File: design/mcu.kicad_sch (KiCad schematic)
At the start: 35 parts, among them J2 SWD_01X06, J3 DEBUG_SPI, U6 STM32H750VBTx, X1 ASTX-H11-25.000MHZ-T, X2 SIT8209AI-21-33S-100.000000X

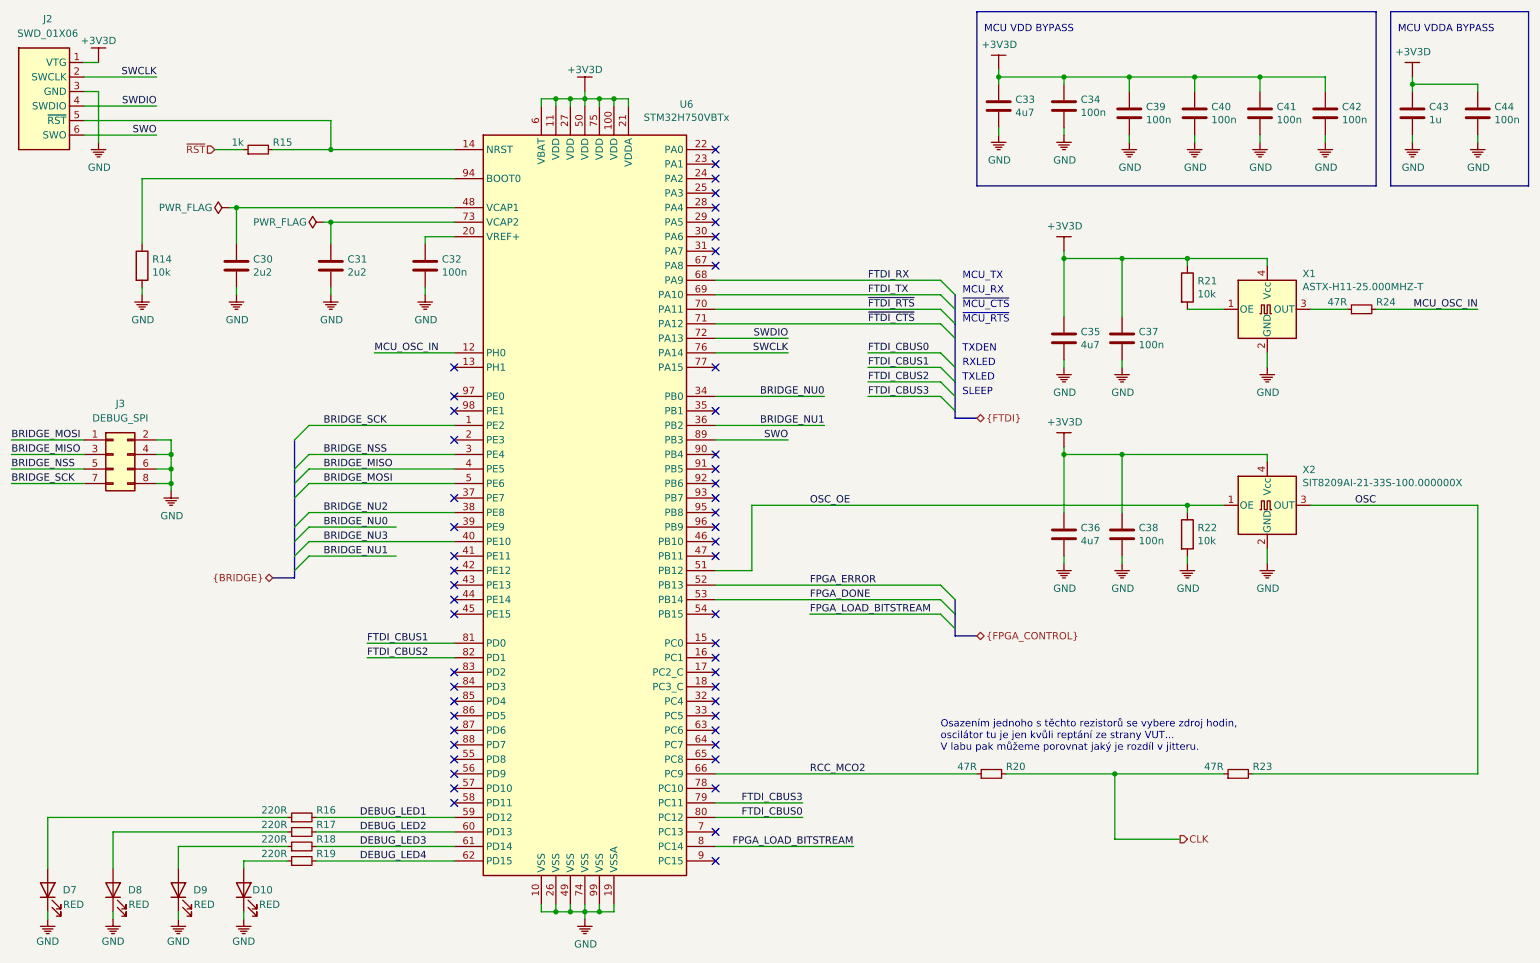
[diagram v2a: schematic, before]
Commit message: Updated reset system
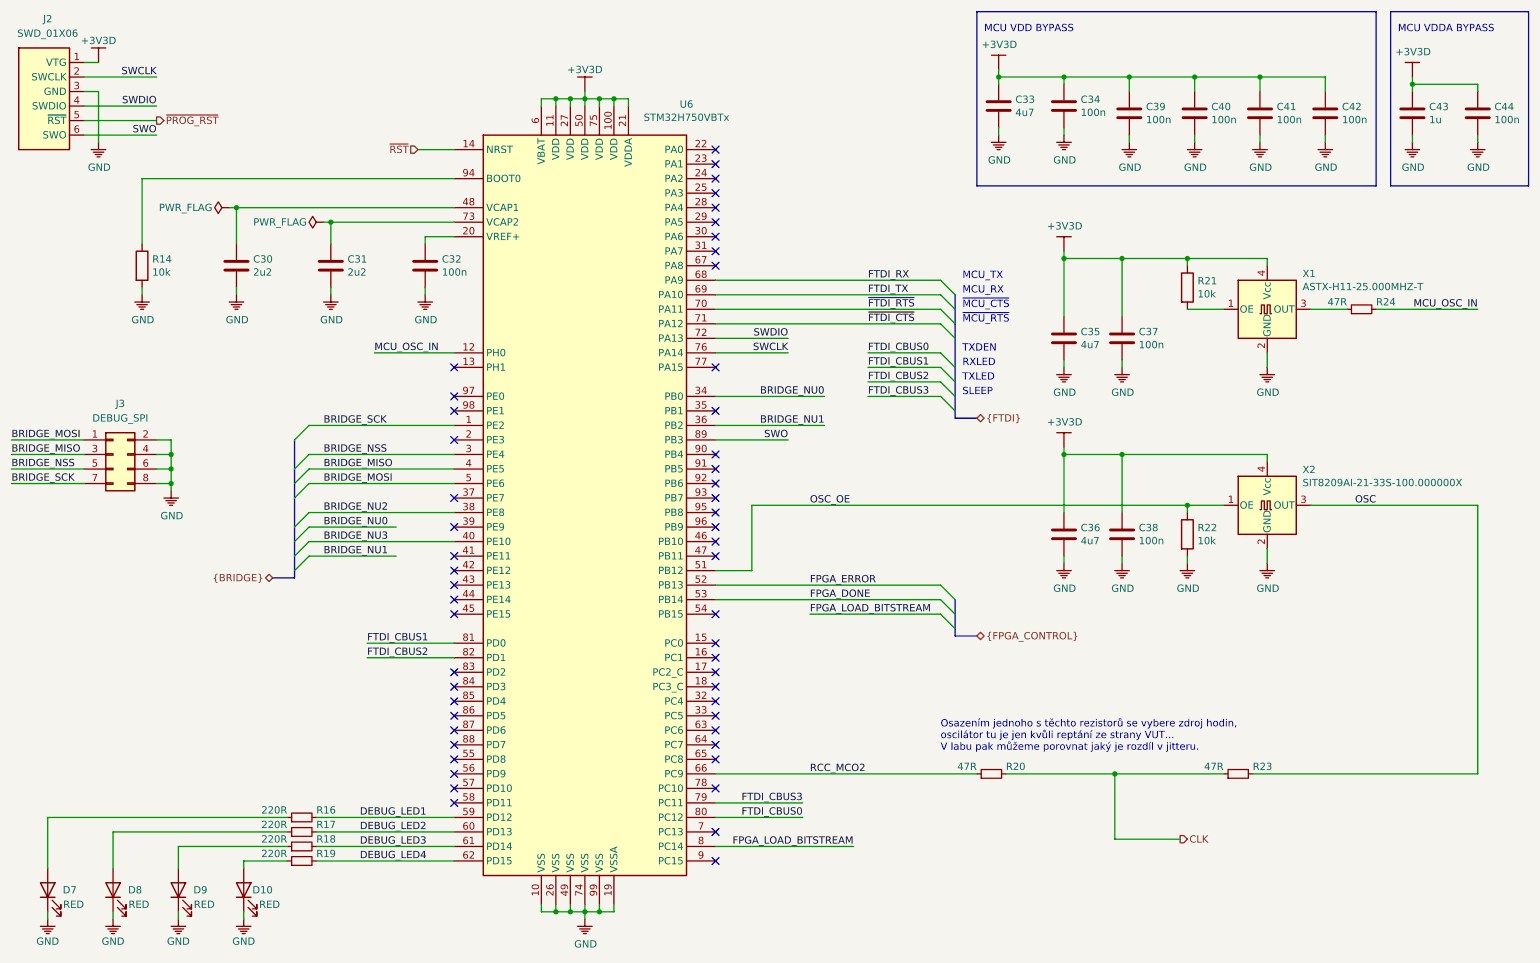
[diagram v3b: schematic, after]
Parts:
- removed R15: 1k, Resistor_SMD:R_0603_1608Metric, symbol Device:R_Small
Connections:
- net ~RST: now also U6.14 (NRST)
- net ~PROG_RST: now reaches J2.5 (~RST)
- net ~PROG_RST: no longer U6.14 (NRST)
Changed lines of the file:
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@@
   (junction (at 45.72 96.52))
   (junction (at 57.15 48.26))
-  (junction (at 73.66 38.1))
   (junction (at 73.66 50.8))
   (junction (at 113.03 29.21))
@@
   (junction (at 236.22 25.4))
   (junction (at 262.89 26.67))
+  (no_connect (at 140.97 43.18))
+  (no_connect (at 140.97 104.14))
+  (no_connect (at 140.97 149.86))
+  (no_connect (at 95.25 139.7))
+  (no_connect (at 95.25 99.06))
+  (no_connect (at 95.25 109.22))
+  (no_connect (at 140.97 134.62))
+  (no_connect (at 140.97 129.54))
+  (no_connect (at 140.97 142.24))
+  (no_connect (at 95.25 134.62))
+  (no_connect (at 95.25 149.86))
+  (no_connect (at 140.97 93.98))
+  (no_connect (at 140.97 53.34))
+  (no_connect (at 140.97 137.16))
+  (no_connect (at 95.25 144.78))
+  (no_connect (at 140.97 76.2))
+  (no_connect (at 95.25 116.84))
+  (no_connect (at 140.97 91.44))
+  (no_connect (at 140.97 38.1))
+  (no_connect (at 95.25 152.4))
+  (no_connect (at 95.25 119.38))
+  (no_connect (at 95.25 137.16))
+  (no_connect (at 140.97 99.06))
+  (no_connect (at 140.97 96.52))
+  (no_connect (at 140.97 124.46))
   (no_connect (at 140.97 45.72))
-  (no_connect (at 140.97 129.54))
-  (no_connect (at 95.25 109.22))
-  (no_connect (at 140.97 93.98))
+  (no_connect (at 140.97 132.08))
+  (no_connect (at 95.25 81.28))
+  (no_connect (at 95.25 104.14))
+  (no_connect (at 95.25 83.82))
+  (no_connect (at 140.97 55.88))
+  (no_connect (at 95.25 111.76))
+  (no_connect (at 140.97 127))
+  (no_connect (at 140.97 50.8))
+  (no_connect (at 140.97 157.48))
+  (no_connect (at 95.25 142.24))
+  (no_connect (at 95.25 76.2))
+  (no_connect (at 140.97 106.68))
+  (no_connect (at 140.97 48.26))
+  (no_connect (at 95.25 88.9))
+  (no_connect (at 140.97 40.64))
+  (no_connect (at 140.97 162.56))
+  (no_connect (at 140.97 109.22))
+  (no_connect (at 140.97 83.82))
+  (no_connect (at 95.25 147.32))
+  (no_connect (at 140.97 144.78))
+  (no_connect (at 140.97 101.6))
+  (no_connect (at 140.97 139.7))
+  (no_connect (at 95.25 114.3))
   (no_connect (at 95.25 132.08))
-  (no_connect (at 95.25 104.14))
-  (no_connect (at 140.97 48.26))
-  (no_connect (at 140.97 53.34))
-  (no_connect (at 140.97 142.24))
-  (no_connect (at 95.25 139.7))
-  (no_connect (at 140.97 139.7))
-  (no_connect (at 140.97 157.48))
-  (no_connect (at 140.97 106.68))
-  (no_connect (at 140.97 127))
-  (no_connect (at 140.97 137.16))
-  (no_connect (at 140.97 38.1))
-  (no_connect (at 140.97 99.06))
-  (no_connect (at 95.25 83.82))
-  (no_connect (at 95.25 88.9))
-  (no_connect (at 140.97 55.88))
-  (no_connect (at 95.25 81.28))
-  (no_connect (at 140.97 50.8))
-  (no_connect (at 95.25 134.62))
-  (no_connect (at 140.97 91.44))
-  (no_connect (at 140.97 96.52))
-  (no_connect (at 140.97 162.56))
-  (no_connect (at 95.25 76.2))
-  (no_connect (at 95.25 137.16))
+  (no_connect (at 140.97 119.38))
   (no_connect (at 95.25 129.54))
-  (no_connect (at 140.97 43.18))
-  (no_connect (at 95.25 149.86))
-  (no_connect (at 95.25 111.76))
-  (no_connect (at 140.97 76.2))
-  (no_connect (at 140.97 149.86))
-  (no_connect (at 140.97 119.38))
-  (no_connect (at 140.97 134.62))
-  (no_connect (at 140.97 104.14))
-  (no_connect (at 95.25 144.78))
-  (no_connect (at 140.97 144.78))
-  (no_connect (at 95.25 152.4))
-  (no_connect (at 140.97 132.08))
-  (no_connect (at 140.97 109.22))
-  (no_connect (at 140.97 101.6))
   (no_connect (at 140.97 58.42))
-  (no_connect (at 95.25 142.24))
-  (no_connect (at 95.25 114.3))
-  (no_connect (at 95.25 147.32))
-  (no_connect (at 140.97 83.82))
-  (no_connect (at 95.25 99.06))
-  (no_connect (at 95.25 116.84))
-  (no_connect (at 95.25 119.38))
-  (no_connect (at 140.97 124.46))
-  (no_connect (at 140.97 40.64))
   (bus_entry (at 67.31 88.9) (size 2.54 -2.54))
   (bus_entry (at 67.31 93.98) (size 2.54 -2.54))
@@
   (wire (pts (xy 30.48 25.4) (xy 43.18 25.4)))
   (wire (pts (xy 30.48 30.48) (xy 43.18 30.48)))
-  (wire (pts (xy 30.48 33.02) (xy 73.66 33.02)))
+  (wire (pts (xy 30.48 33.02) (xy 43.18 33.02)))
   (wire (pts (xy 30.48 35.56) (xy 43.18 35.56)))
   (wire (pts (xy 33.02 27.94) (xy 30.48 27.94)))
@@
   (wire (pts (xy 46.99 160.02) (xy 46.99 163.83)))
   (wire (pts (xy 46.99 171.45) (xy 46.99 172.72)))
-  (wire (pts (xy 53.34 38.1) (xy 58.42 38.1)))
   (wire (pts (xy 55.88 48.26) (xy 57.15 48.26)))
   (wire (pts (xy 57.15 48.26) (xy 57.15 54.61)))
@@
   (wire (pts (xy 58.42 162.56) (xy 58.42 163.83)))
   (wire (pts (xy 58.42 171.45) (xy 58.42 172.72)))
-  (wire (pts (xy 63.5 38.1) (xy 73.66 38.1)))
   (wire (pts (xy 66.04 154.94) (xy 24.13 154.94)))
   (wire (pts (xy 66.04 157.48) (xy 35.56 157.48)))
@@
   (wire (pts (xy 69.85 109.22) (xy 85.09 109.22)))
   (wire (pts (xy 72.39 50.8) (xy 73.66 50.8)))
-  (wire (pts (xy 73.66 33.02) (xy 73.66 38.1)))
-  (wire (pts (xy 73.66 38.1) (xy 95.25 38.1)))
   (wire (pts (xy 73.66 50.8) (xy 73.66 54.61)))
   (wire (pts (xy 73.66 50.8) (xy 95.25 50.8)))
@@
   (wire (pts (xy 80.01 127) (xy 95.25 127)))
   (wire (pts (xy 81.28 73.66) (xy 95.25 73.66)))
+  (wire (pts (xy 88.9 38.1) (xy 95.25 38.1)))
   (wire (pts (xy 90.17 53.34) (xy 95.25 53.34)))
   (wire (pts (xy 90.17 54.61) (xy 90.17 53.34)))
@@
   (bus (pts (xy 63.5 113.03) (xy 67.31 113.03)))
   (bus (pts (xy 67.31 88.9) (xy 67.31 96.52)))
-  (bus (pts (xy 67.31 96.52) (xy 67.31 104.14)))
-  (bus (pts (xy 67.31 104.14) (xy 67.31 109.22)))
-  (bus (pts (xy 67.31 109.22) (xy 67.31 113.03)))
+  (bus (pts (xy 67.31 96.52) (xy 67.31 99.06)))
+  (bus (pts (xy 67.31 99.06) (xy 67.31 106.68)))
+  (bus (pts (xy 67.31 106.68) (xy 67.31 111.76)))
+  (bus (pts (xy 67.31 111.76) (xy 67.31 113.03)))
   (bus (pts (xy 182.88 63.5) (xy 182.88 68.58)))
   (bus (pts (xy 182.88 68.58) (xy 182.88 76.2)))
-  (bus (pts (xy 182.88 76.2) (xy 182.88 78.74)))
-  (bus (pts (xy 182.88 78.74) (xy 182.88 83.82)))
-  (bus (pts (xy 182.88 83.82) (xy 182.88 85.09)))
+  (bus (pts (xy 182.88 76.2) (xy 182.88 81.28)))
+  (bus (pts (xy 182.88 81.28) (xy 182.88 85.09)))
   (bus (pts (xy 182.88 85.09) (xy 186.69 85.09)))
-  (bus (pts (xy 182.88 116.84) (xy 182.88 119.38)))
-  (bus (pts (xy 182.88 119.38) (xy 182.88 123.19)))
+  (bus (pts (xy 182.88 116.84) (xy 182.88 121.92)))
+  (bus (pts (xy 182.88 121.92) (xy 182.88 123.19)))
   (bus (pts (xy 186.69 123.19) (xy 182.88 123.19)))
   (polyline (pts (xy 186.69 13.97) (xy 186.69 44.45)))
@@
     (effects (font (size 1.27 1.27)) (justify right bottom))
   )
-  (hierarchical_label "~RST" (shape input) (at 53.34 38.1 180)
-    (effects (font (size 1.27 1.27)) (justify right))
+  (hierarchical_label "~PROG_RST" (shape output) (at 43.18 33.02 0)
+    (effects (font (size 1.27 1.27)) (justify left))
   )
   (hierarchical_label "{BRIDGE}" (shape bidirectional) (at 63.5 113.03 180)
     (effects (font (size 1.27 1.27)) (justify right))
   )
+  (hierarchical_label "~RST" (shape input) (at 88.9 38.1 180)
+    (effects (font (size 1.27 1.27)) (justify right))
+  )
   (hierarchical_label "{FTDI}" (shape bidirectional) (at 186.69 85.09 0)
     (effects (font (size 1.27 1.27)) (justify left))
@@
       (effects (font (size 1.27 1.27)) hide)
     )
-  )
-  (symbol (lib_name "Device:R_Small_1") (lib_id "Device:R_Small") (at 60.96 38.1 90) (unit 1)
-    (property "Reference" "R15" (id 0) (at 63.5 36.83 90)
-      (effects (font (size 1.27 1.27)) (justify right))
-    )
-    (property "Value" "1k" (id 1) (at 58.42 36.83 90)
-      (effects (font (size 1.27 1.27)) (justify left))
-    )
-    (property "Footprint" "Resistor_SMD:R_0603_1608Metric" (id 2) (at 60.96 38.1 0)
-      (effects (font (size 1.27 1.27)) hide)
-    )
-    (property "Datasheet" "~" (id 3) (at 60.96 38.1 0)
-      (effects (font (size 1.27 1.27)) hide)
-    )

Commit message: Added fiducials
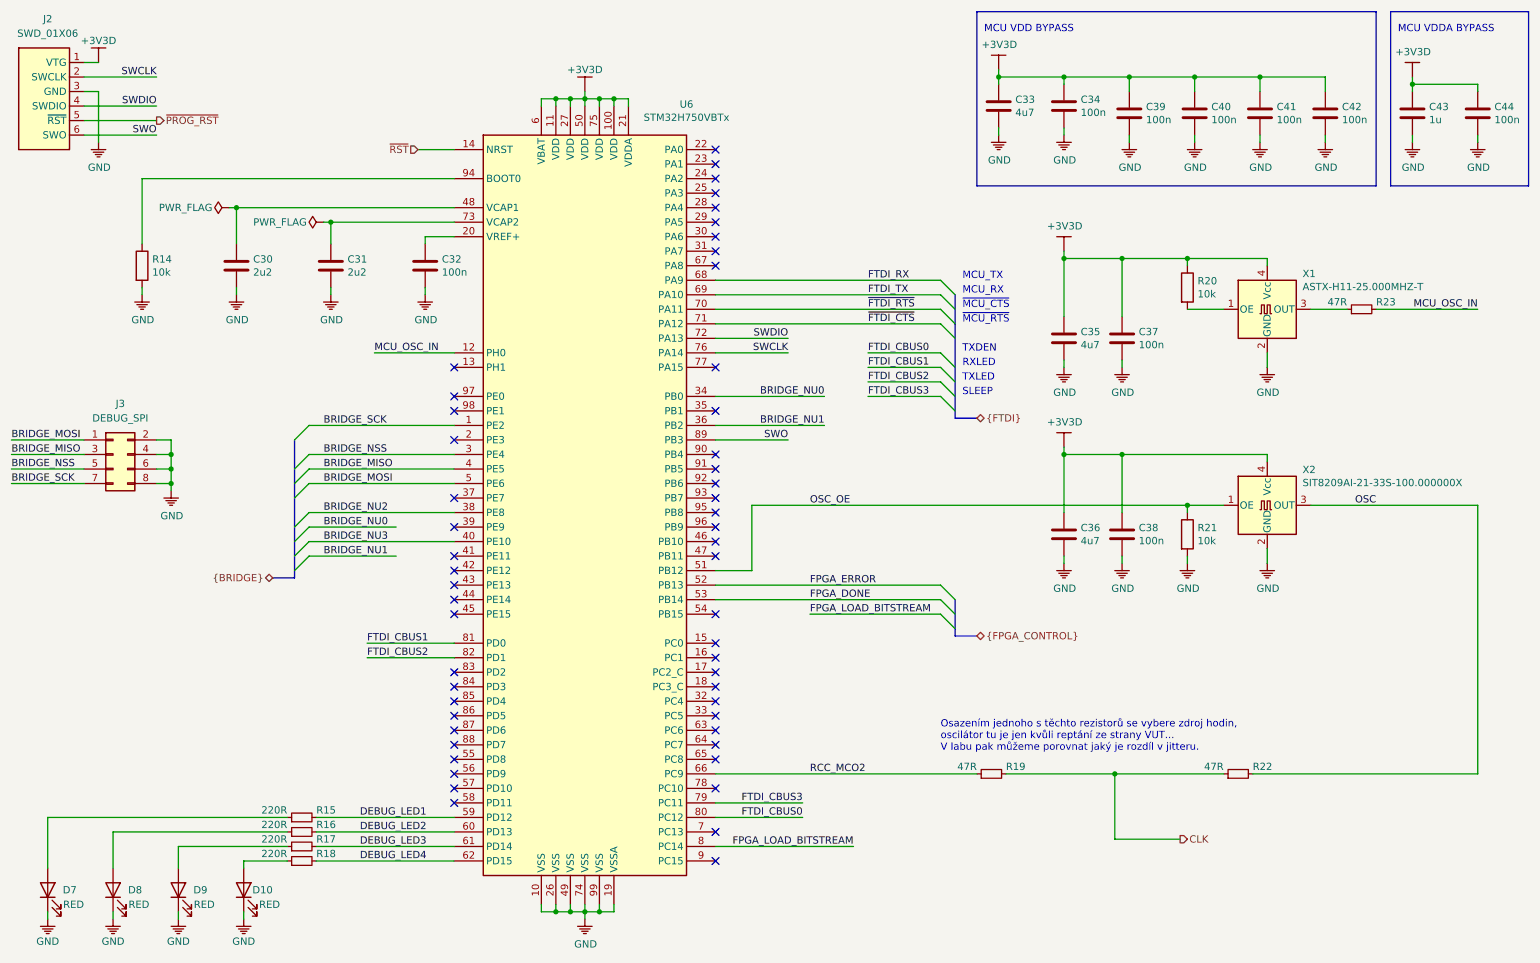
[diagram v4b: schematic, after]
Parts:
- renumbered R16 to R15, R17 to R16, R18 to R17, R19 to R18, R20 to R19, R21 to R20, R22 to R21, R23 to R22, R24 to R23

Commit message: Updated schematic
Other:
- note added: "Osazením jednoho s těchto rezistorů se vybere zdroj hodin, oscilátor je tu kvůli případným problémům s jitterem MCO."
- note removed: "Osazením jednoho s těchto rezistorů se vybere zdroj hodin, oscilátor tu je jen kvůli reptání ze strany VUT... V labu pak můžeme porovnat jaký je rozdíl v jitteru."
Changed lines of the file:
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@@
   (junction (at 236.22 25.4))
   (junction (at 262.89 26.67))
+  (no_connect (at 95.25 116.84))
+  (no_connect (at 140.97 48.26))
+  (no_connect (at 140.97 91.44))
+  (no_connect (at 95.25 152.4))
+  (no_connect (at 95.25 144.78))
+  (no_connect (at 140.97 96.52))
+  (no_connect (at 140.97 83.82))
+  (no_connect (at 140.97 58.42))
+  (no_connect (at 95.25 129.54))
+  (no_connect (at 140.97 93.98))
   (no_connect (at 140.97 43.18))
-  (no_connect (at 140.97 104.14))
+  (no_connect (at 95.25 132.08))
+  (no_connect (at 140.97 109.22))
+  (no_connect (at 140.97 134.62))
+  (no_connect (at 140.97 132.08))
+  (no_connect (at 140.97 129.54))
+  (no_connect (at 95.25 119.38))
+  (no_connect (at 140.97 119.38))
+  (no_connect (at 140.97 137.16))
+  (no_connect (at 140.97 101.6))
+  (no_connect (at 140.97 124.46))
+  (no_connect (at 95.25 137.16))
   (no_connect (at 140.97 149.86))
-  (no_connect (at 95.25 139.7))
+  (no_connect (at 140.97 45.72))
+  (no_connect (at 140.97 106.68))
+  (no_connect (at 140.97 53.34))
+  (no_connect (at 95.25 88.9))
+  (no_connect (at 95.25 109.22))
+  (no_connect (at 95.25 147.32))
+  (no_connect (at 140.97 76.2))
   (no_connect (at 95.25 99.06))
-  (no_connect (at 95.25 109.22))
-  (no_connect (at 140.97 134.62))
-  (no_connect (at 140.97 129.54))
+  (no_connect (at 140.97 50.8))
+  (no_connect (at 95.25 111.76))
+  (no_connect (at 95.25 76.2))
+  (no_connect (at 140.97 99.06))
   (no_connect (at 140.97 142.24))
   (no_connect (at 95.25 134.62))
+  (no_connect (at 95.25 104.14))
+  (no_connect (at 140.97 127))
   (no_connect (at 95.25 149.86))
-  (no_connect (at 140.97 93.98))
-  (no_connect (at 140.97 53.34))
-  (no_connect (at 140.97 137.16))
-  (no_connect (at 95.25 144.78))
-  (no_connect (at 140.97 76.2))
-  (no_connect (at 95.25 116.84))
-  (no_connect (at 140.97 91.44))
+  (no_connect (at 95.25 142.24))
+  (no_connect (at 95.25 83.82))
   (no_connect (at 140.97 38.1))
-  (no_connect (at 95.25 152.4))
-  (no_connect (at 95.25 119.38))
-  (no_connect (at 95.25 137.16))
-  (no_connect (at 140.97 99.06))
-  (no_connect (at 140.97 96.52))
-  (no_connect (at 140.97 124.46))
-  (no_connect (at 140.97 45.72))
-  (no_connect (at 140.97 132.08))
+  (no_connect (at 95.25 139.7))
+  (no_connect (at 140.97 157.48))
   (no_connect (at 95.25 81.28))
-  (no_connect (at 95.25 104.14))
-  (no_connect (at 95.25 83.82))
+  (no_connect (at 140.97 104.14))
+  (no_connect (at 140.97 144.78))
+  (no_connect (at 140.97 139.7))
+  (no_connect (at 140.97 162.56))
+  (no_connect (at 140.97 40.64))
+  (no_connect (at 95.25 114.3))
   (no_connect (at 140.97 55.88))
-  (no_connect (at 95.25 111.76))
-  (no_connect (at 140.97 127))
-  (no_connect (at 140.97 50.8))
-  (no_connect (at 140.97 157.48))
-  (no_connect (at 95.25 142.24))
-  (no_connect (at 95.25 76.2))
-  (no_connect (at 140.97 106.68))
-  (no_connect (at 140.97 48.26))
-  (no_connect (at 95.25 88.9))
-  (no_connect (at 140.97 40.64))
-  (no_connect (at 140.97 162.56))
-  (no_connect (at 140.97 109.22))
-  (no_connect (at 140.97 83.82))
-  (no_connect (at 95.25 147.32))
-  (no_connect (at 140.97 144.78))
-  (no_connect (at 140.97 101.6))
-  (no_connect (at 140.97 139.7))
-  (no_connect (at 95.25 114.3))
-  (no_connect (at 95.25 132.08))
-  (no_connect (at 140.97 119.38))
-  (no_connect (at 95.25 129.54))
-  (no_connect (at 140.97 58.42))
   (bus_entry (at 67.31 88.9) (size 2.54 -2.54))
   (bus_entry (at 67.31 93.98) (size 2.54 -2.54))
@@
   (bus (pts (xy 67.31 106.68) (xy 67.31 111.76)))
   (bus (pts (xy 67.31 111.76) (xy 67.31 113.03)))
-  (bus (pts (xy 182.88 63.5) (xy 182.88 68.58)))
-  (bus (pts (xy 182.88 68.58) (xy 182.88 76.2)))
-  (bus (pts (xy 182.88 76.2) (xy 182.88 81.28)))
+  (bus (pts (xy 182.88 63.5) (xy 182.88 66.04)))
+  (bus (pts (xy 182.88 66.04) (xy 182.88 71.12)))
+  (bus (pts (xy 182.88 71.12) (xy 182.88 78.74)))
+  (bus (pts (xy 182.88 78.74) (xy 182.88 81.28)))
   (bus (pts (xy 182.88 81.28) (xy 182.88 85.09)))
   (bus (pts (xy 182.88 85.09) (xy 186.69 85.09)))
@@
   (polyline (pts (xy 283.21 13.97) (xy 283.21 44.45)))
   (polyline (pts (xy 283.21 44.45) (xy 259.08 44.45)))
-  (text "Osazením jednoho s těchto rezistorů se vybere zdroj hodin,\noscilátor tu je jen kvůli reptání ze strany VUT...\nV labu pak můžeme porovnat jaký je rozdíl v jitteru."
+  (text "Osazením jednoho s těchto rezistorů se vybere zdroj hodin,\noscilátor je tu kvůli případným problémům s jitterem MCO."
     (at 180.34 143.51 0)
     (effects (font (size 1.27 1.27)) (justify left bottom))
